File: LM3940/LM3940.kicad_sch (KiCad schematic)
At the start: 9 parts, among them U1 LM317L_SOT-89

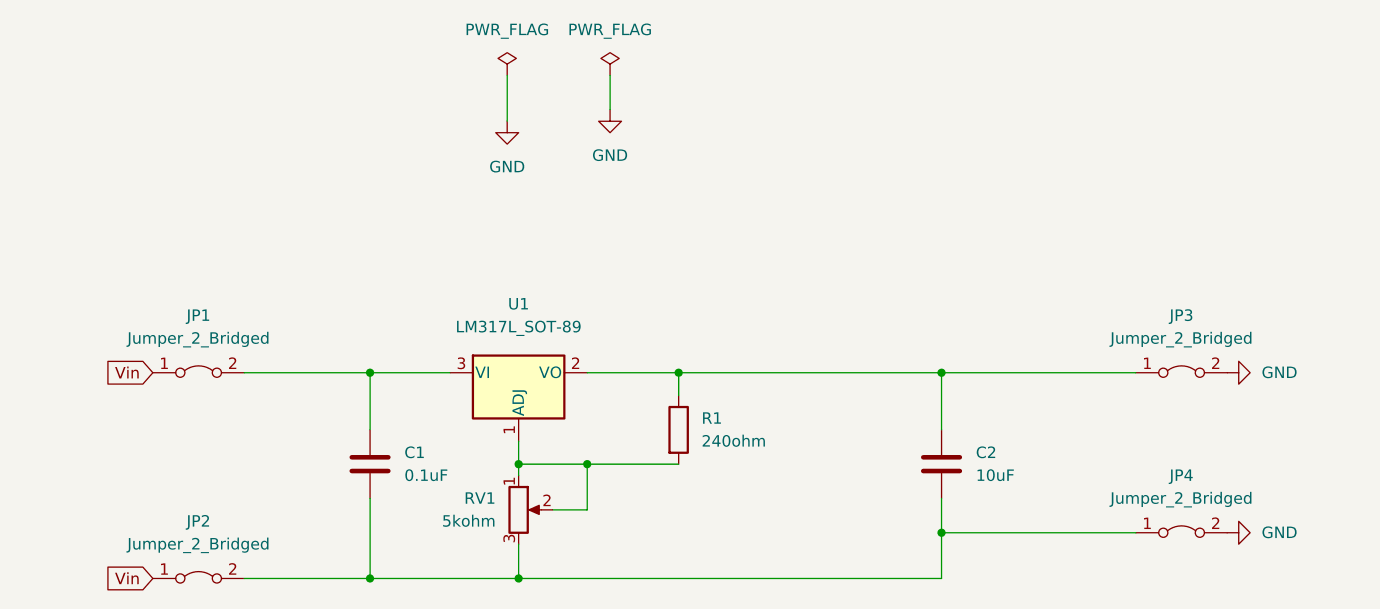
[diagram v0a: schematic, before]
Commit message: Errore nel pin 3 del transistor
Tutti gli errori sono stati eliminati, resta solo uno, quello nel pin 3 (Vin) del transistor.
Non trovo una soluzione
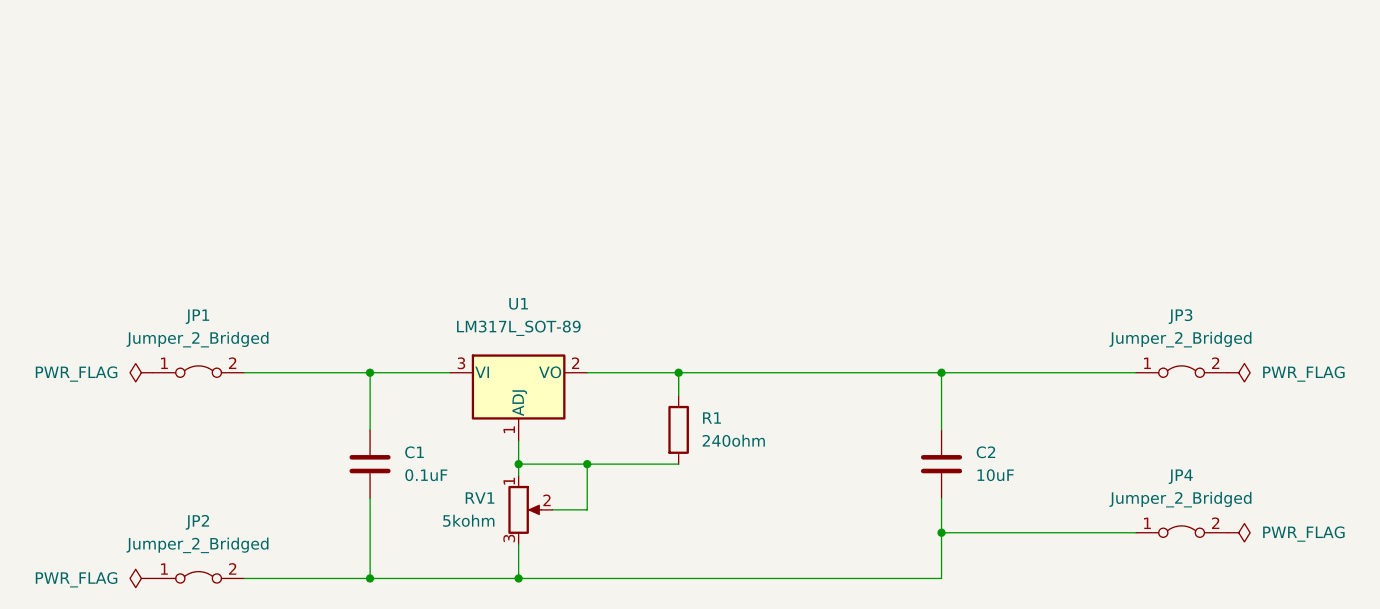
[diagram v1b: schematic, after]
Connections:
- net GND: no longer names the net of JP4.2 (B)
- net GND: no longer JP3.2 (B)
- net Vin: no longer names the net of JP2.1 (A)
- net Vin: no longer JP1.1 (A)
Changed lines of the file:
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@@
-    (stroke (width 0) (type default) (color 0 0 0 0))
-  )
-  (wire (pts (xy 105.41 27.94) (xy 105.41 33.02))
     (stroke (width 0) (type default) (color 0 0 0 0))
   )
@@
   (wire (pts (xy 153.67 60.96) (xy 153.67 67.31))
     (stroke (width 0) (type default) (color 0 0 0 0))
-  )
-  (wire (pts (xy 116.84 27.94) (xy 116.84 31.75))
-    (stroke (width 0) (type default) (color 0 0 0 0))
-  )
-  (global_label "Vin" (shape input) (at 66.04 60.96 180) (fields_autoplaced)
-    (effects (font (size 1.27 1.27)) (justify right))
-    (property "Intersheet References" "${INTERSHEET_REFS}" (id 0) (at 60.7845 60.8806 0)
-      (effects (font (size 1.27 1.27)) (justify right) hide)
-    )
-  )
-  (global_label "Vin" (shape input) (at 66.04 83.82 180) (fields_autoplaced)
-    (effects (font (size 1.27 1.27)) (justify right))
-    (property "Intersheet References" "${INTERSHEET_REFS}" (id 0) (at 60.7845 83.7406 0)
-      (effects (font (size 1.27 1.27)) (justify right) hide)
-    )
   )
   (symbol (lib_id "Jumper:Jumper_2_Bridged") (at 71.12 83.82 0) (unit 1)
@@
     (pin "2")
   )
-  (symbol (lib_id "power:GND") (at 185.42 78.74 90) (unit 1)
-    (in_bom yes) (on_board yes) (fields_autoplaced)
-    (property "Reference" "#PWR0103" (id 0) (at 191.77 78.74 0)
-      (effects (font (size 1.27 1.27)) hide)
-    )
-    (property "Value" "GND" (id 1) (at 189.23 78.7399 90)
-      (effects (font (size 1.27 1.27)) (justify right))
+  (symbol (lib_id "power:PWR_FLAG") (at 185.42 78.74 270) (unit 1)
+    (in_bom yes) (on_board yes) (fields_autoplaced)
+    (property "Reference" "#FLG0101" (id 0) (at 187.325 78.74 0)
+      (effects (font (size 1.27 1.27)) hide)
+    )
+    (property "Value" "PWR_FLAG" (id 1) (at 189.23 78.7399 90)
+      (effects (font (size 1.27 1.27)) (justify left))
     )
     (property "Footprint" "" (id 2) (at 185.42 78.74 0)
       (effects (font (size 1.27 1.27)) hide)
     )
-    (property "Datasheet" "" (id 3) (at 185.42 78.74 0)
+    (property "Datasheet" "~" (id 3) (at 185.42 78.74 0)
       (effects (font (size 1.27 1.27)) hide)
     )
@@
     (pin "1")
     (pin "2")
-  )
-  (symbol (lib_id "power:GND") (at 105.41 33.02 0) (unit 1)
-    (in_bom yes) (on_board yes) (fields_autoplaced)
-    (property "Reference" "#PWR0104" (id 0) (at 105.41 39.37 0)
-      (effects (font (size 1.27 1.27)) hide)
-    )
-    (property "Value" "GND" (id 1) (at 105.41 38.1 0))
-    (property "Footprint" "" (id 2) (at 105.41 33.02 0)
-      (effects (font (size 1.27 1.27)) hide)
-    )
-    (property "Datasheet" "" (id 3) (at 105.41 33.02 0)
-      (effects (font (size 1.27 1.27)) hide)
-    )
-    (pin "1")
   )
   (symbol (lib_id "Device:R_Potentiometer") (at 106.68 76.2 0) (unit 1)
@@
     (pin "2")
   )
-  (symbol (lib_id "power:PWR_FLAG") (at 105.41 27.94 0) (unit 1)
-    (in_bom yes) (on_board yes) (fields_autoplaced)
-    (property "Reference" "#FLG0102" (id 0) (at 105.41 26.035 0)
-      (effects (font (size 1.27 1.27)) hide)
-    )
-    (property "Value" "PWR_FLAG" (id 1) (at 105.41 22.86 0))
-    (property "Footprint" "" (id 2) (at 105.41 27.94 0)
-      (effects (font (size 1.27 1.27)) hide)
-    )
-    (property "Datasheet" "~" (id 3) (at 105.41 27.94 0)
+  (symbol (lib_id "power:PWR_FLAG") (at 66.04 60.96 90) (unit 1)
+    (in_bom yes) (on_board yes) (fields_autoplaced)
+    (property "Reference" "#FLG01" (id 0) (at 64.135 60.96 0)
+      (effects (font (size 1.27 1.27)) hide)
+    )
+    (property "Value" "PWR_FLAG" (id 1) (at 62.23 60.9599 90)
+      (effects (font (size 1.27 1.27)) (justify left))
+    )
+    (property "Footprint" "" (id 2) (at 66.04 60.96 0)
+      (effects (font (size 1.27 1.27)) hide)
+    )
+    (property "Datasheet" "~" (id 3) (at 66.04 60.96 0)
+      (effects (font (size 1.27 1.27)) hide)
+    )
+    (pin "1")
+  )
+  (symbol (lib_id "power:PWR_FLAG") (at 185.42 60.96 270) (unit 1)
+    (in_bom yes) (on_board yes) (fields_autoplaced)
+    (property "Reference" "#FLG0102" (id 0) (at 187.325 60.96 0)
+      (effects (font (size 1.27 1.27)) hide)
+    )
+    (property "Value" "PWR_FLAG" (id 1) (at 189.23 60.9599 90)
+      (effects (font (size 1.27 1.27)) (justify left))
+    )
+    (property "Footprint" "" (id 2) (at 185.42 60.96 0)
+      (effects (font (size 1.27 1.27)) hide)
+    )
+    (property "Datasheet" "~" (id 3) (at 185.42 60.96 0)
       (effects (font (size 1.27 1.27)) hide)
     )
@@
     (pin "2")
   )
-  (symbol (lib_id "power:GND") (at 185.42 60.96 90) (unit 1)
-    (in_bom yes) (on_board yes) (fields_autoplaced)
-    (property "Reference" "#PWR0102" (id 0) (at 191.77 60.96 0)
-      (effects (font (size 1.27 1.27)) hide)
-    )
-    (property "Value" "GND" (id 1) (at 189.23 60.9599 90)
-      (effects (font (size 1.27 1.27)) (justify right))
-    )
-    (property "Footprint" "" (id 2) (at 185.42 60.96 0)
-      (effects (font (size 1.27 1.27)) hide)
-    )
-    (property "Datasheet" "" (id 3) (at 185.42 60.96 0)
-      (effects (font (size 1.27 1.27)) hide)
-    )
-    (pin "1")
-  )
   (symbol (lib_id "Jumper:Jumper_2_Bridged") (at 180.34 60.96 0) (unit 1)
     (in_bom yes) (on_board yes) (fields_autoplaced)
@@
     (pin "2")
   )
-  (symbol (lib_id "power:PWR_FLAG") (at 116.84 27.94 0) (unit 1)
-    (in_bom yes) (on_board yes) (fields_autoplaced)
-    (property "Reference" "#FLG0101" (id 0) (at 116.84 26.035 0)
-      (effects (font (size 1.27 1.27)) hide)
-    )
-    (property "Value" "PWR_FLAG" (id 1) (at 116.84 22.86 0))
-    (property "Footprint" "" (id 2) (at 116.84 27.94 0)
-      (effects (font (size 1.27 1.27)) hide)
-    )
-    (property "Datasheet" "~" (id 3) (at 116.84 27.94 0)
-      (effects (font (size 1.27 1.27)) hide)
-    )
-    (pin "1")
-  )
-  (symbol (lib_id "power:GND") (at 116.84 31.75 0) (unit 1)
-    (in_bom yes) (on_board yes) (fields_autoplaced)
-    (property "Reference" "#PWR0101" (id 0) (at 116.84 38.1 0)
-      (effects (font (size 1.27 1.27)) hide)
-    )
-    (property "Value" "GND" (id 1) (at 116.84 36.83 0))
-    (property "Footprint" "" (id 2) (at 116.84 31.75 0)
-      (effects (font (size 1.27 1.27)) hide)
-    )
-    (property "Datasheet" "" (id 3) (at 116.84 31.75 0)
+  (symbol (lib_id "power:PWR_FLAG") (at 66.04 83.82 90) (unit 1)
+    (in_bom yes) (on_board yes) (fields_autoplaced)
+    (property "Reference" "#FLG02" (id 0) (at 64.135 83.82 0)
+      (effects (font (size 1.27 1.27)) hide)
+    )
+    (property "Value" "PWR_FLAG" (id 1) (at 62.23 83.8199 90)
+      (effects (font (size 1.27 1.27)) (justify left))
+    )
+    (property "Footprint" "" (id 2) (at 66.04 83.82 0)
+      (effects (font (size 1.27 1.27)) hide)
+    )
+    (property "Datasheet" "~" (id 3) (at 66.04 83.82 0)
       (effects (font (size 1.27 1.27)) hide)
     )
@@
   )
   (symbol_instances
-    (path "/8d19ca86-6402-4c7e-9bc1-ea8e92b91f84"
+    (path "/497c002e-b7be-4902-ae97-2a0cc5efffd5"
+      (reference "#FLG01") (unit 1) (value "PWR_FLAG") (footprint "")
+    )
+    (path "/8019743b-3243-4a1e-a2cc-44572adb5cf7"
+      (reference "#FLG02") (unit 1) (value "PWR_FLAG") (footprint "")
+    )
+    (path "/088cb663-ab5c-45ad-9c60-4ce7bfcb2e82"
       (reference "#FLG0101") (unit 1) (value "PWR_FLAG") (footprint "")
     )
-    (path "/5d47973c-5789-455b-b5a1-19a522e725f9"
+    (path "/5cf4b660-b2e9-4da4-a6b7-c4399ea04a91"
       (reference "#FLG0102") (unit 1) (value "PWR_FLAG") (footprint "")
     )
-    (path "/91c71f6f-289b-4c9d-9cbc-566d0c15228d"
-      (reference "#PWR0101") (unit 1) (value "GND") (footprint "")
-    )
-    (path "/625099ef-f050-42f6-ae1b-f5242f2663af"
-      (reference "#PWR0102") (unit 1) (value "GND") (footprint "")
-    )
-    (path "/12b92dab-e465-4b58-8170-59107de8b61a"
-      (reference "#PWR0103") (unit 1) (value "GND") (footprint "")
-    )
-    (path "/1e3b9742-213b-44a1-93ae-5daad03090c7"
-      (reference "#PWR0104") (unit 1) (value "GND") (footprint "")
-    )
     (path "/16827c54-c9b4-4ced-9372-0aa6bd8a5213"
